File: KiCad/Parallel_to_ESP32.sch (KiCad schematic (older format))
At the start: 21 parts, among them J1 DB25_Male, J2 Micro_SD_Card_Socket, J3 Conn_01x02, J4 Conn_01x02, U1 ESP32-DEVKIT-V1, U2 SN74CB3T16210

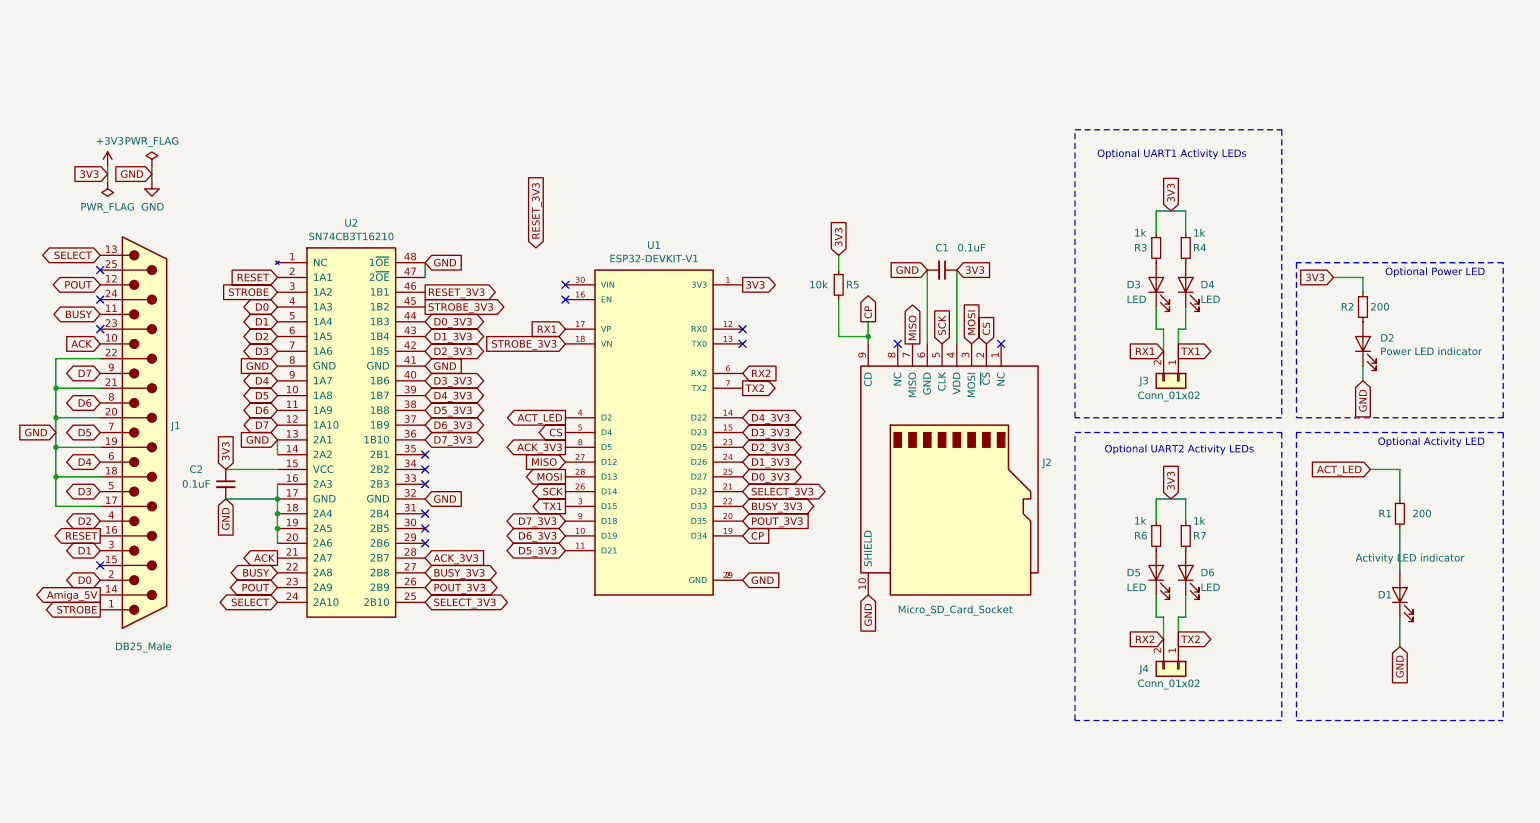
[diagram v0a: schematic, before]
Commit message: Added jumper JP1 for RESET-signal (optional)
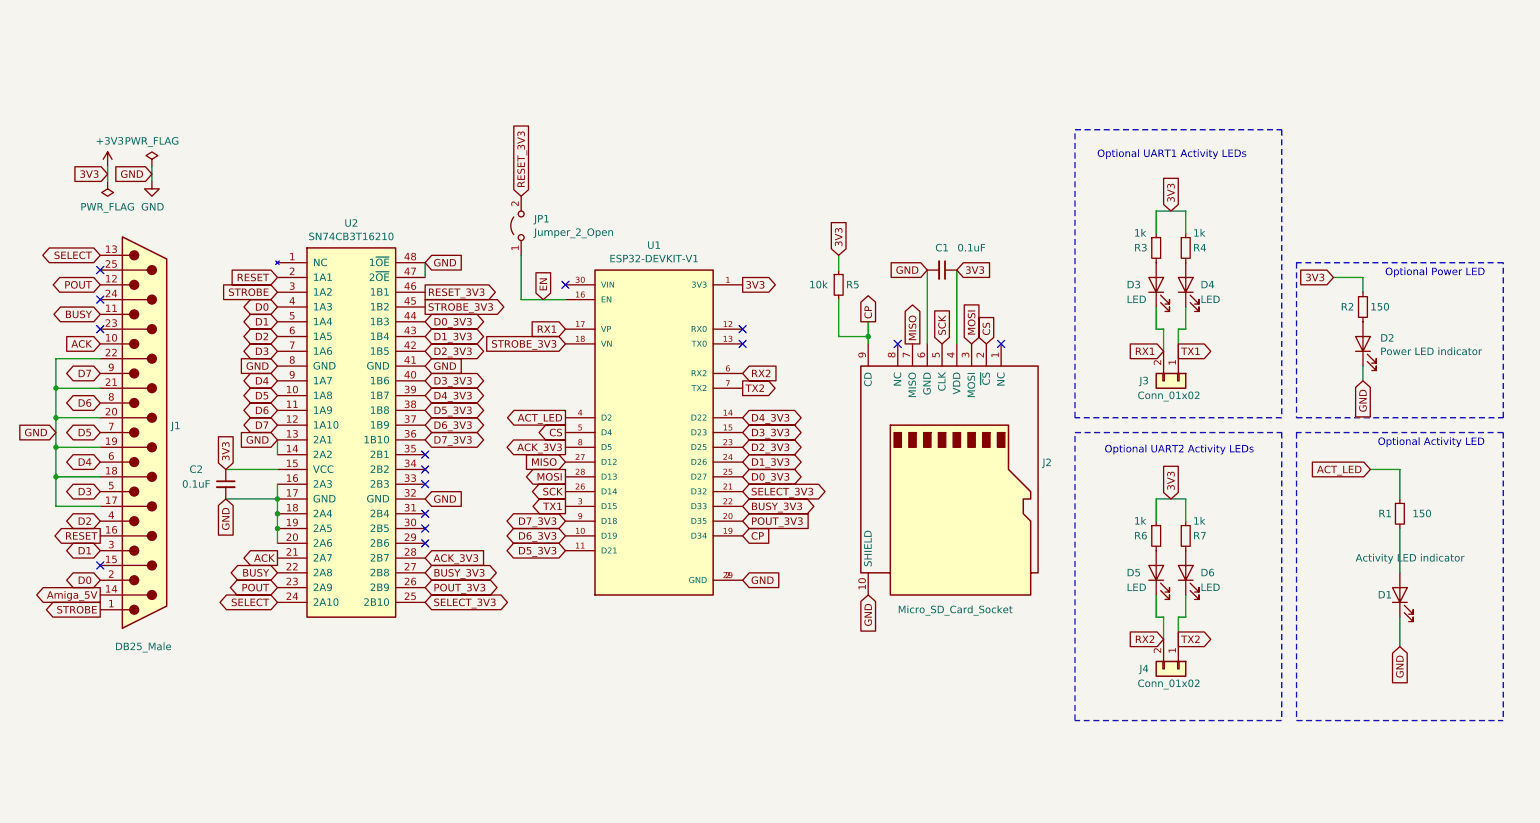
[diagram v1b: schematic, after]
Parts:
- added JP1: Jumper_2_Open, Resistor_SMD:R_1206_3216Metric_Pad1.42x1.75mm_HandSolder, symbol Jumper:Jumper_2_Open
- R1, R2: value 200 -> 150
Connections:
- net RESET_3V3: now also JP1.2 (B)
- net EN: now reaches U1.16 (EN)
- net EN: now also JP1.1 (A)
- no-connect marks 16 -> 15
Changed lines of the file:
@@
 P 10100 3350
 F 0 "R2" H 9950 3350 50  0000 L CNN
-F 1 "200" H 10150 3350 50  0000 L CNN
+F 1 "150" H 10150 3350 50  0000 L CNN
 F 2 "Resistor_SMD:R_0805_2012Metric_Pad1.15x1.40mm_HandSolder" H 10100 3350 50  0001 C CNN
 F 3 "~" H 10100 3350 50  0001 C CNN
@@
 Text GLabel 4700 4800 0    50   BiDi ~ 0
 D7_3V3
-NoConn ~ 4700 3300
 Text GLabel 4700 3600 0    50   Input ~ 0
 STROBE_3V3
-Text GLabel 4500 2950 1    50   Input ~ 0
+Text GLabel 4400 2600 1    50   Input ~ 0
 RESET_3V3
 Text GLabel 3750 3050 2    50   Input ~ 0
@@
 P 10350 4750
 F 0 "R1" H 10250 4750 50  0000 C CNN
-F 1 "200" H 10500 4750 50  0000 C CNN
+F 1 "150" H 10500 4750 50  0000 C CNN
 F 2 "Resistor_SMD:R_0805_2012Metric_Pad1.15x1.40mm_HandSolder" H 10350 4750 50  0001 C CNN
 F 3 "~" H 10350 4750 50  0001 C CNN
@@
 Text GLabel 4700 4100 0    50   Output ~ 0
 ACT_LED
+$Comp
+L Jumper:Jumper_2_Open JP1
+U 1 1 6466A6DB
+P 4400 2800
+F 0 "JP1" V 4446 2712 50  0000 R CNN
+F 1 "Jumper_2_Open" V 4355 2712 50  0000 R CNN
+F 2 "Resistor_SMD:R_1206_3216Metric_Pad1.42x1.75mm_HandSolder" H 4400 2800 50  0001 C CNN
+F 3 "~" H 4400 2800 50  0001 C CNN
+	1    4400 2800
+	0    -1   -1   0
+$EndComp
+Wire Wire Line
+	4700 3300 4400 3300
+Wire Wire Line
+	4400 3300 4400 3000
+Text GLabel 4550 3300 1    50   Input ~ 0
+EN
 $EndSCHEMATC

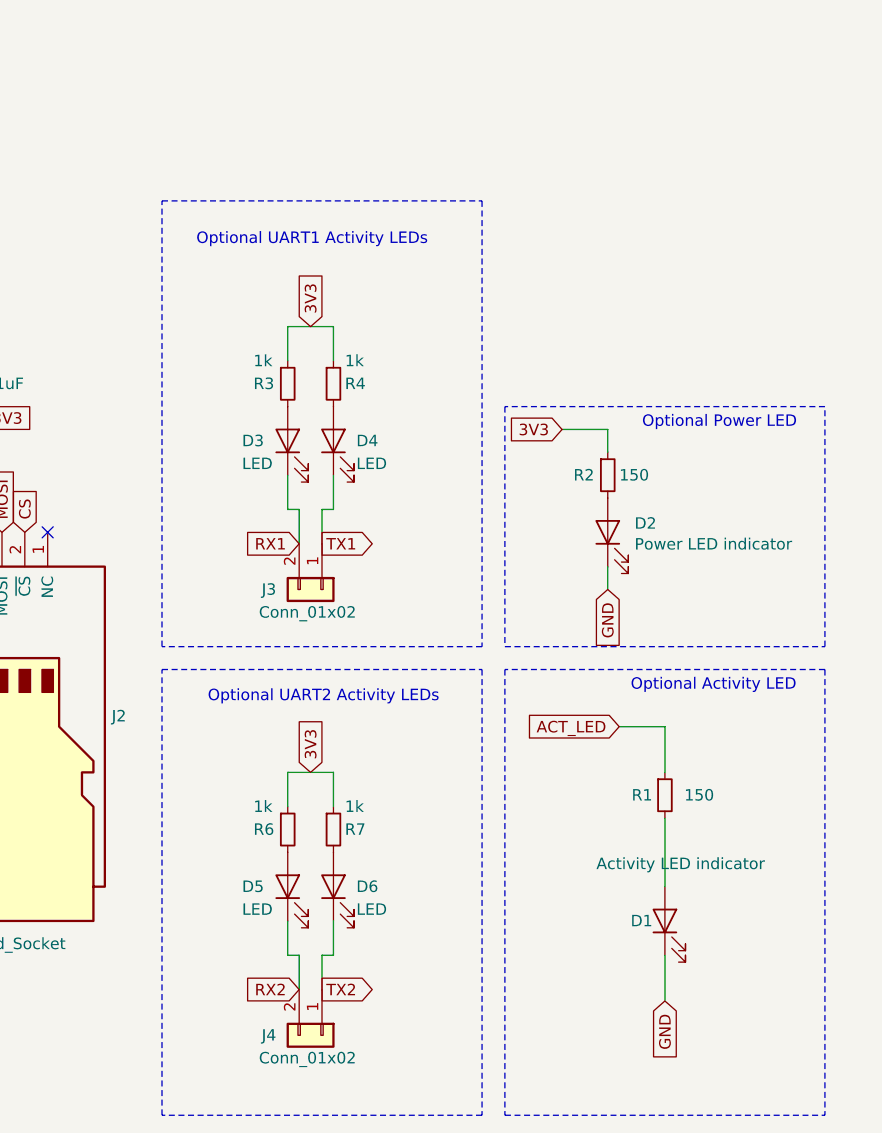
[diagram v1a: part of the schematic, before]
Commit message: Changed to surface mount footprint for UART1 and UART2 and 3V3/GND on underside, changed JP1 to regular PinHeader P2.54mm
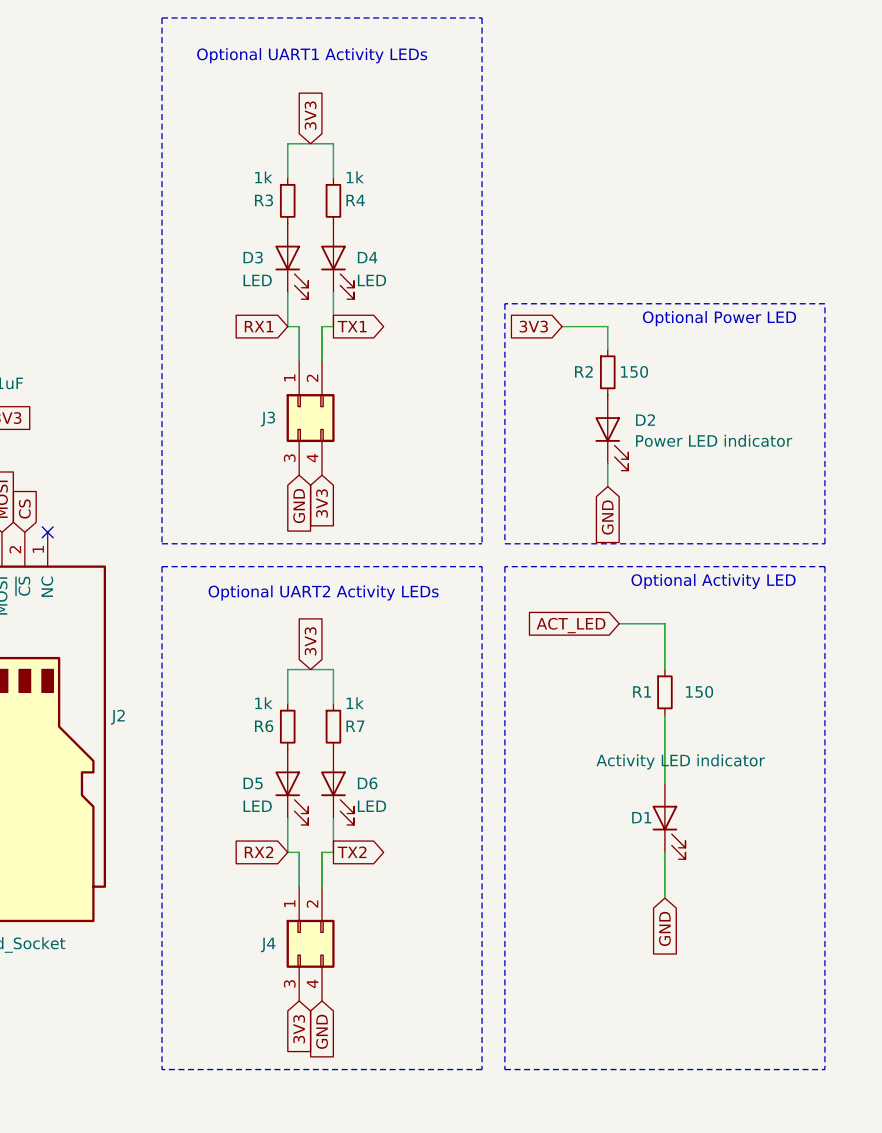
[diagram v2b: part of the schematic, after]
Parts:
- removed J3, J4: Conn_01x02, Connector_PinHeader_2.54mm:PinHeader_1x02_P2.54mm_Vertical, symbol Connector_Generic:Conn_01x02
- added J3, J4: Conn_02x02_Top_Bottom, Parallel_to_ESP32:PinHeader_2x02_P2.54mm_EdgeMount_SMD, symbol Connector_Generic:Conn_02x02_Top_Bottom
- JP1: footprint Resistor_SMD:R_1206_3216Metric_Pad1.42x1.75mm_HandSolder -> Connector_PinHeader_2.54mm:PinHeader_1x02_P2.54mm_Vertical
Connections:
- net +3V3: now also J3.4 (Pin_4), J4.3 (Pin_3)
- net GND: now also J3.3 (Pin_3), J4.4 (Pin_4)
- net RX1: now also J3.1 (Pin_1)
- net RX2: now also J4.1 (Pin_1)
- net TX1: now also J3.2 (Pin_2)
- net TX2: now also J4.2 (Pin_2)
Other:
- moved on the sheet: D1, D2, D3, D4, D5, D6, R1, R2, R3, R4, R6, R7

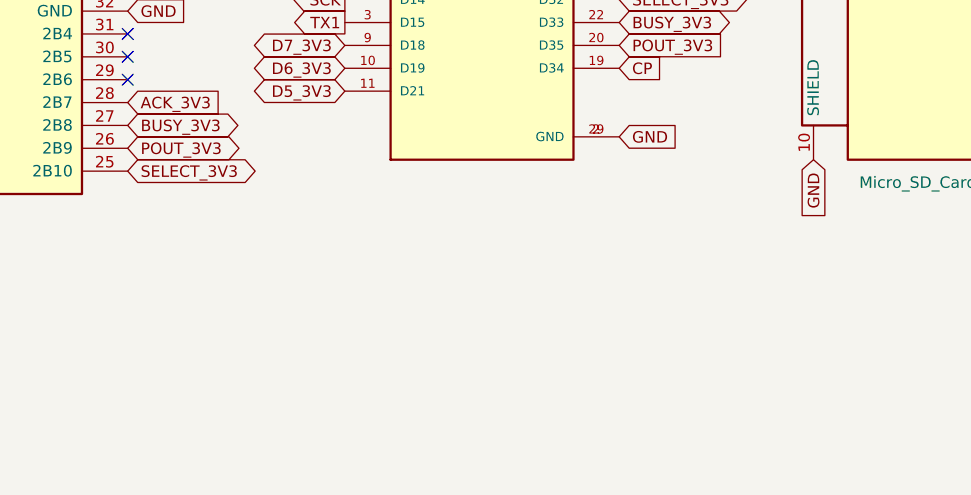
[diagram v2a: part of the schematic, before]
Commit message: Added optional pull-up resistor packs for all Parallel-port-signals pulled up by Amigas 5V (pin 14)
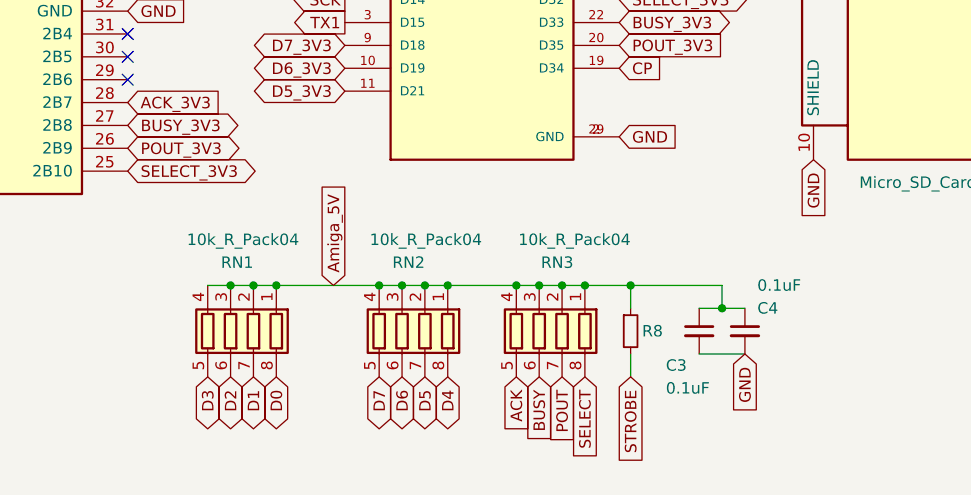
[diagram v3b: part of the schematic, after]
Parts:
- added C3, C4: 0.1uF, Capacitor_SMD:C_0805_2012Metric_Pad1.15x1.40mm_HandSolder, symbol Device:C_Small
- added R8: 10k, Resistor_SMD:R_0603_1608Metric_Pad1.05x0.95mm_HandSolder, symbol Device:R_Small
- added RN1, RN2, RN3: 10k_R_Pack04, Parallel_to_ESP32:RESCAF80P320X160X60-8N, symbol Device:R_Pack04
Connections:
- net ACK: now also RN3.5 (R4.2)
- net Amiga_5V: now also C3.1, C4.1, R8.1, RN1.1 (R1.1), RN1.2 (R2.1), RN1.3 (R3.1), RN1.4 (R4.1), RN2.1 (R1.1), RN2.2 (R2.1), RN2.3 (R3.1), RN2.4 (R4.1), RN3.1 (R1.1), RN3.2 (R2.1), RN3.3 (R3.1), RN3.4 (R4.1)
- net BUSY: now also RN3.6 (R3.2)
- net D0: now also RN1.8 (R1.2)
- net D1: now also RN1.7 (R2.2)
- net D2: now also RN1.6 (R3.2)
- net D3: now also RN1.5 (R4.2)
- net D4: now also RN2.8 (R1.2)
- net D5: now also RN2.7 (R2.2)
- net D6: now also RN2.6 (R3.2)
- net D7: now also RN2.5 (R4.2)
- net GND: now also C3.2, C4.2
- net POUT: now also RN3.7 (R2.2)
- net SELECT: now also RN3.8 (R1.2)
- net STROBE: now also R8.2
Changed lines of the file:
@@
 Wire Notes Line
 	11050 3750 11050 5950
+$Comp
+L Device:R_Pack04 RN3
+U 1 1 6470ED39
+P 5550 6050
+F 0 "RN3" H 5400 5750 50  0000 L CNN
+F 1 "10k_R_Pack04" H 5150 5650 50  0000 L CNN
+F 2 "Parallel_to_ESP32:RESCAF80P320X160X60-8N" V 5825 6050 50  0001 C CNN
+F 3 "~" H 5550 6050 50  0001 C CNN
+	1    5550 6050
+	-1   0    0    1
+$EndComp
+Text GLabel 5750 6250 3    50   Input ~ 0
+SELECT
+Text GLabel 5650 6250 3    50   Input ~ 0
+POUT
+Text GLabel 5550 6250 3    50   Input ~ 0
+BUSY
+Text GLabel 5450 6250 3    50   Input ~ 0
+ACK
+Wire Wire Line
+	5450 5850 5550 5850
+Connection ~ 5550 5850
+Connection ~ 5650 5850
+Wire Wire Line
+	5650 5850 5750 5850
+Wire Wire Line
+	5550 5850 5650 5850
+$Comp
+L Device:R_Pack04 RN1
+U 1 1 6473FA68
+P 4200 6050
+F 0 "RN1" H 4100 5750 50  0000 L CNN
+F 1 "10k_R_Pack04" H 3900 5650 50  0000 L CNN
+F 2 "Parallel_to_ESP32:RESCAF80P320X160X60-8N" V 4475 6050 50  0001 C CNN
+F 3 "~" H 4200 6050 50  0001 C CNN
+	1    4200 6050
+	-1   0    0    1
+$EndComp
+Wire Wire Line
+	4100 5850 4200 5850
+Connection ~ 4200 5850
+Wire Wire Line
+	4200 5850 4300 5850
+Connection ~ 4300 5850
+Wire Wire Line
+	4300 5850 4400 5850
+Text GLabel 4400 6250 3    50   BiDi ~ 0
+D0
+Text GLabel 4300 6250 3    50   BiDi ~ 0
+D1
+Text GLabel 4200 6250 3    50   BiDi ~ 0
+D2
+Text GLabel 4100 6250 3    50   BiDi ~ 0
+D3
+Text GLabel 5950 6250 3    50   Input ~ 0
+STROBE
+Text GLabel 4950 6250 3    50   BiDi ~ 0
+D6
+Text GLabel 4850 6250 3    50   BiDi ~ 0
+D7
+Text GLabel 5150 6250 3    50   BiDi ~ 0
+D4
+Text GLabel 5050 6250 3    50   BiDi ~ 0
+D5
+$Comp
+L Device:R_Pack04 RN2
+U 1 1 6474C6A2
+P 4950 6050
+F 0 "RN2" H 4850 5750 50  0000 L CNN
+F 1 "10k_R_Pack04" H 4600 5650 50  0000 L CNN
+F 2 "Parallel_to_ESP32:RESCAF80P320X160X60-8N" V 5225 6050 50  0001 C CNN
+F 3 "~" H 4950 6050 50  0001 C CNN
+	1    4950 6050
+	-1   0    0    1
+$EndComp
+Text GLabel 4650 5850 1    50   Input ~ 0
+Amiga_5V
+Wire Wire Line
+	4850 5850 4950 5850
+Connection ~ 4950 5850
+Wire Wire Line
+	4950 5850 5050 5850
+Connection ~ 5050 5850
+Wire Wire Line
+	5050 5850 5150 5850
+$Comp
+L Device:R_Small R8
+U 1 1 647840C8
+P 5950 6050
+F 0 "R8" H 6000 6050 50  0000 L CNN
+F 1 "10k" H 5750 6050 50  0001 L CNN
+F 2 "Resistor_SMD:R_0603_1608Metric_Pad1.05x0.95mm_HandSolder" H 5950 6050 50  0001 C CNN
+F 3 "~" H 5950 6050 50  0001 C CNN
+	1    5950 6050
+	1    0    0    -1
+$EndComp
+Wire Wire Line
+	5950 5950 5950 5850
+Wire Wire Line
+	5950 6150 5950 6250
+$Comp
+L Device:C_Small C3
+U 1 1 6479390B
+P 6250 6050
+F 0 "C3" H 6150 5900 50  0000 C CNN
+F 1 "0.1uF" H 6200 5800 50  0000 C CNN
+F 2 "Capacitor_SMD:C_0805_2012Metric_Pad1.15x1.40mm_HandSolder" H 6250 6050 50  0001 C CNN
+F 3 "~" H 6250 6050 50  0001 C CNN
+	1    6250 6050
+	1    0    0    -1
+$EndComp
+$Comp
+L Device:C_Small C4
+U 1 1 647A00BF
+P 6450 6050
+F 0 "C4" H 6550 6150 50  0000 C CNN
+F 1 "0.1uF" H 6600 6250 50  0000 C CNN
+F 2 "Capacitor_SMD:C_0805_2012Metric_Pad1.15x1.40mm_HandSolder" H 6450 6050 50  0001 C CNN
+F 3 "~" H 6450 6050 50  0001 C CNN
+	1    6450 6050
+	1    0    0    -1
+$EndComp
+Wire Wire Line
+	6250 5950 6350 5950
+Text GLabel 6450 6150 3    50   Input ~ 0
+GND
+Wire Wire Line
+	6250 6150 6450 6150
+Wire Wire Line
+	6350 5850 6350 5950
+Connection ~ 5950 5850
+Wire Wire Line
+	5950 5850 6350 5850
+Connection ~ 6350 5950
+Wire Wire Line
+	6350 5950 6450 5950
+Wire Wire Line
+	4400 5850 4850 5850
+Connection ~ 4400 5850
+Connection ~ 4850 5850
+Wire Wire Line
+	5150 5850 5450 5850
+Connection ~ 5150 5850
+Connection ~ 5450 5850
+Wire Wire Line
+	5750 5850 5950 5850
+Connection ~ 5750 5850
 $EndSCHEMATC

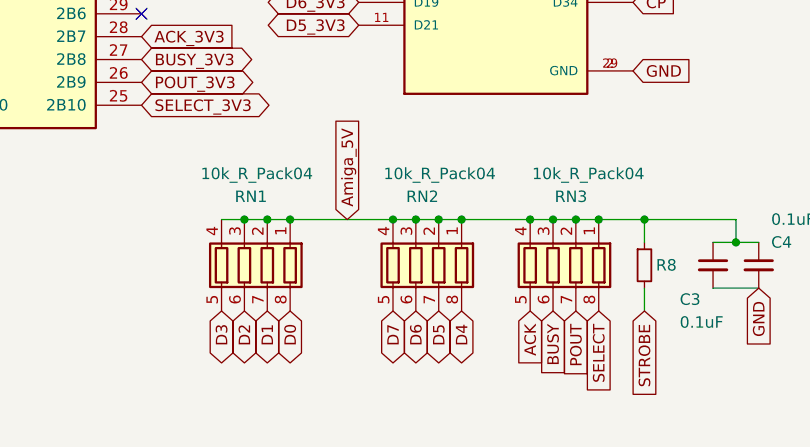
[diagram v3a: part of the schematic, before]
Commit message: Changed pull-up resistor packs to value 4.7k (cay16-4701f4lf)
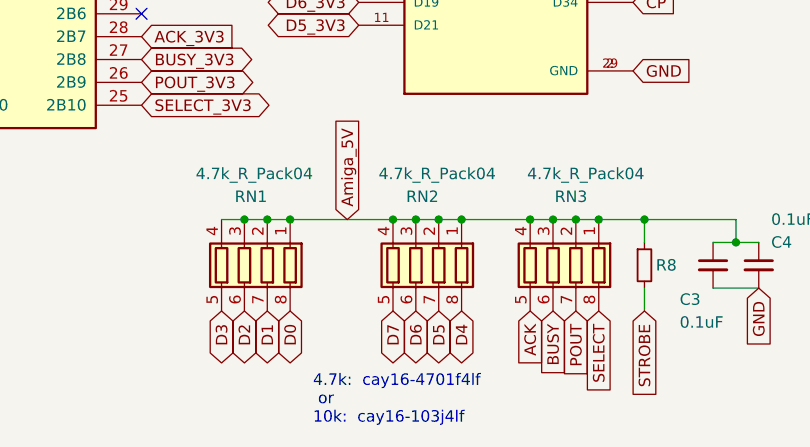
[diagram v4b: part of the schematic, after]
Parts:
- RN1, RN2, RN3: value 10k_R_Pack04 -> 4.7k_R_Pack04
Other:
- note added: "4.7k: cay16-4701f4lf\n or\n10k: cay16-103j4lf"
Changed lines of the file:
@@
 P 5550 6050
 F 0 "RN3" H 5400 5750 50  0000 L CNN
-F 1 "10k_R_Pack04" H 5150 5650 50  0000 L CNN
+F 1 "4.7k_R_Pack04" H 5150 5650 50  0000 L CNN
 F 2 "Parallel_to_ESP32:RESCAF80P320X160X60-8N" V 5825 6050 50  0001 C CNN
 F 3 "~" H 5550 6050 50  0001 C CNN
@@
 P 4200 6050
 F 0 "RN1" H 4100 5750 50  0000 L CNN
-F 1 "10k_R_Pack04" H 3900 5650 50  0000 L CNN
+F 1 "4.7k_R_Pack04" H 3900 5650 50  0000 L CNN
 F 2 "Parallel_to_ESP32:RESCAF80P320X160X60-8N" V 4475 6050 50  0001 C CNN
 F 3 "~" H 4200 6050 50  0001 C CNN
@@
 P 4950 6050
 F 0 "RN2" H 4850 5750 50  0000 L CNN
-F 1 "10k_R_Pack04" H 4600 5650 50  0000 L CNN
+F 1 "4.7k_R_Pack04" H 4600 5650 50  0000 L CNN
 F 2 "Parallel_to_ESP32:RESCAF80P320X160X60-8N" V 5225 6050 50  0001 C CNN
 F 3 "~" H 4950 6050 50  0001 C CNN
@@
 	5750 5850 5950 5850
 Connection ~ 5750 5850
+Text Notes 4500 6750 0    50   ~ 0
+4.7k:  cay16-4701f4lf\n or\n10k:  cay16-103j4lf
 $EndSCHEMATC
